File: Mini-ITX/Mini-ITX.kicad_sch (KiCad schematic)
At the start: 8 parts

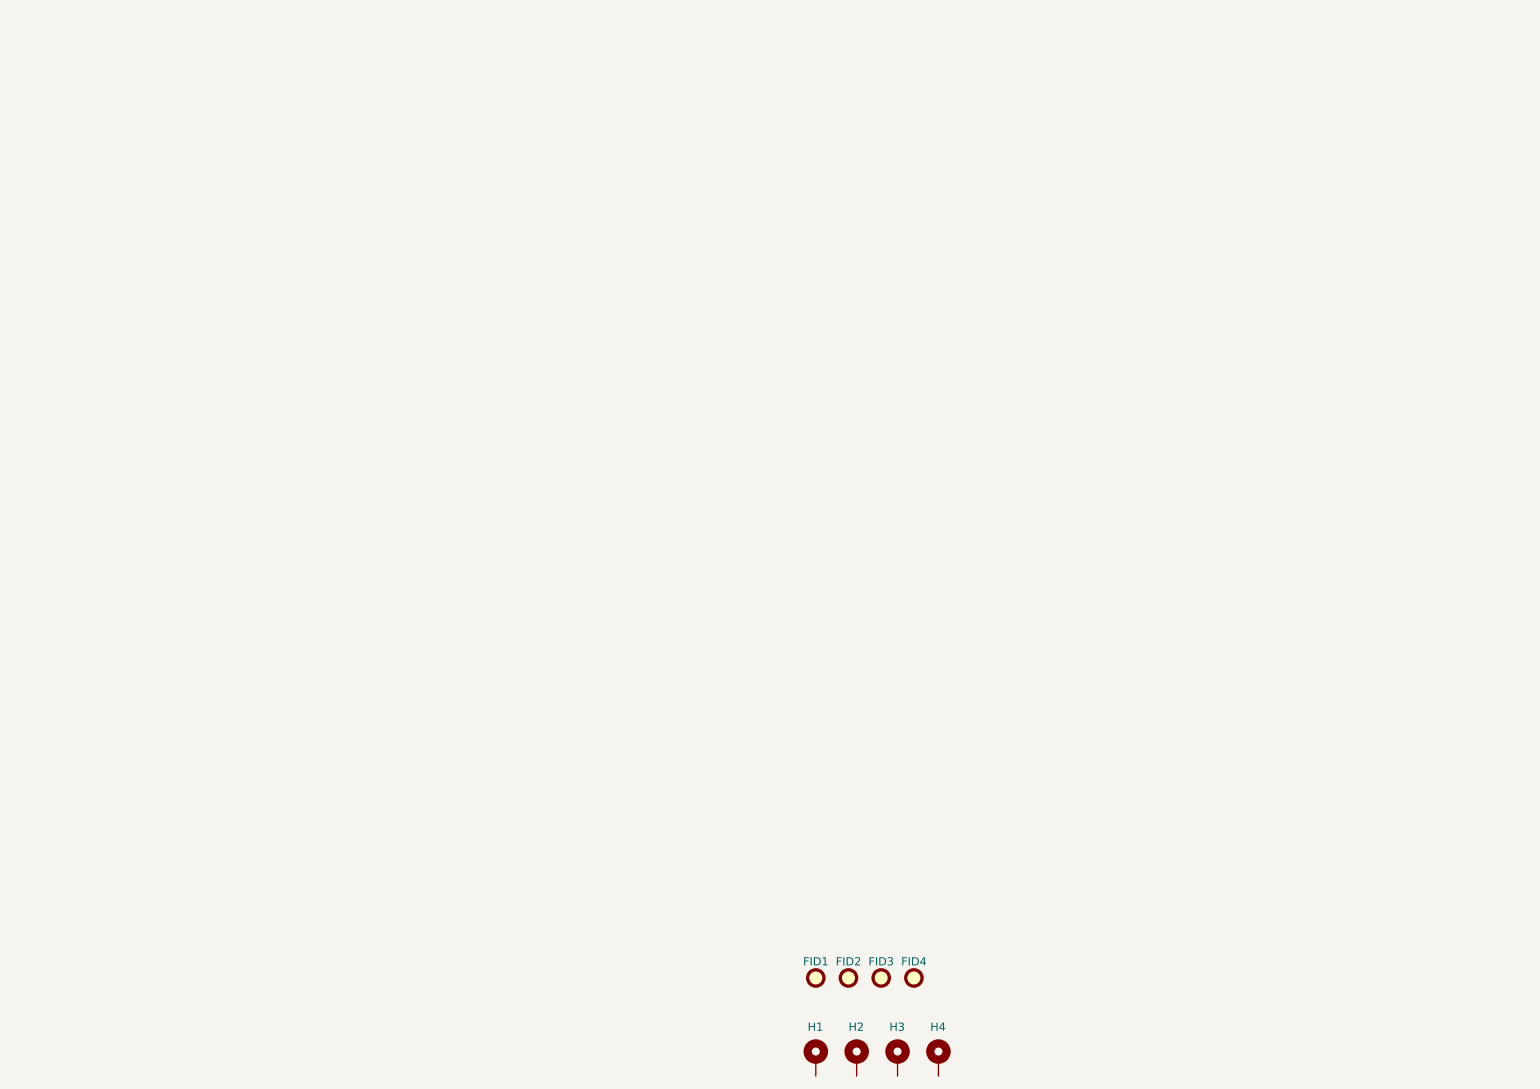
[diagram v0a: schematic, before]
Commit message: add common motherboard connectors
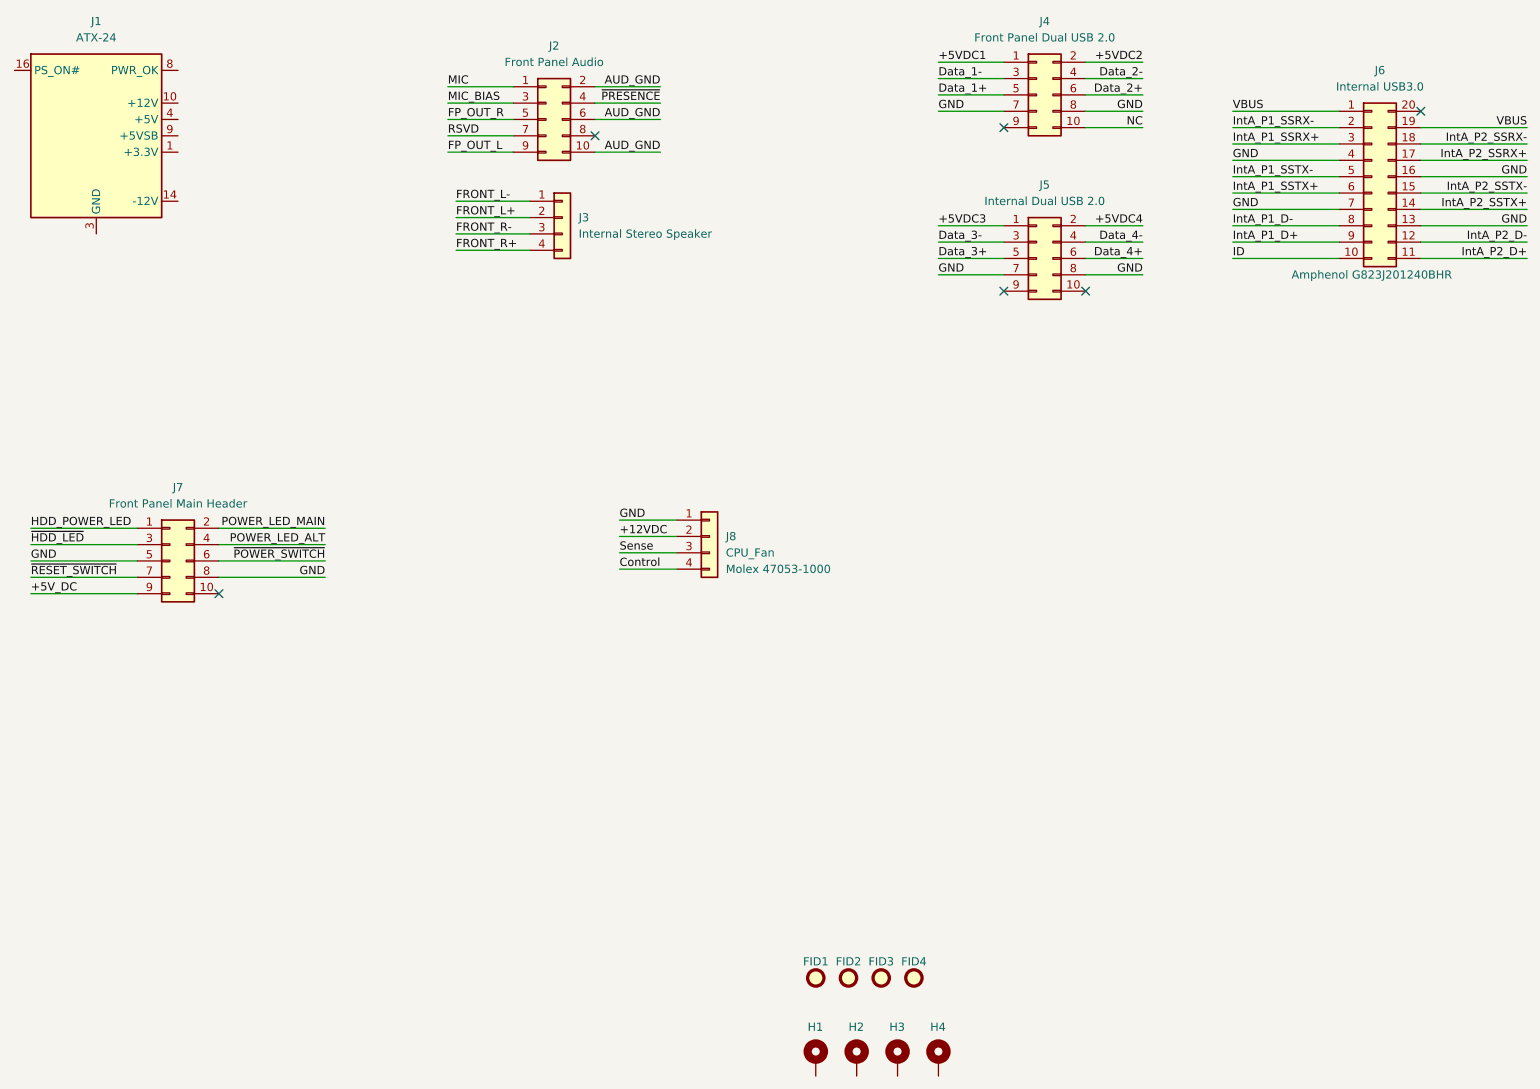
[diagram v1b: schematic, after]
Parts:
- added J1: ATX-24, Connector_Molex:Molex_Mini-Fit_Jr_5566-24A_2x12_P4.20mm_Vertical, symbol Connector:ATX-24
- added J2: Front Panel Audio, Connector_PinHeader_2.54mm:PinHeader_2x05_P2.54mm_Vertical, symbol Connector_Generic:Conn_02x05_Odd_Even
- added J3: Internal Stereo Speaker, Connector_Computer:CS_JS-1125-04_1x04_P2.00mm_Vertical, symbol Connector_Generic:Conn_01x04
- added J4: Front Panel Dual USB 2.0, Connector_PinHeader_2.54mm:PinHeader_2x05_P2.54mm_Vertical, symbol Connector_Generic:Conn_02x05_Odd_Even
- added J5: Internal Dual USB 2.0, Connector_PinHeader_2.54mm:PinHeader_2x05_P2.54mm_Vertical, symbol Connector_Generic:Conn_02x05_Odd_Even
- added J6: Internal USB3.0, Connector_Computer:Amphenol_G823J201xx0xHR_2x10_P2.00mm_Vertical, symbol Connector_Generic:Conn_02x10_Counter_Clockwise
- added J7: Front Panel Main Header, Connector_PinHeader_2.54mm:PinHeader_2x05_P2.54mm_Vertical, symbol Connector_Generic:Conn_02x05_Odd_Even
- added J8: CPU_Fan, Connector:FanPinHeader_1x04_P2.54mm_Vertical, symbol Connector_Generic:Conn_01x04
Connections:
- new net: J1.1 (+3.3V), J1.12 (+3.3V), J1.13 (+3.3V), J1.2 (+3.3V)
- new net: J1.10 (+12V), J1.11 (+12V)
- new net: J1.15 (GND), J1.17 (GND), J1.18 (GND), J1.19 (GND), J1.24 (GND), J1.3 (GND), J1.5 (GND), J1.7 (GND)
- new net: J1.21 (+5V), J1.22 (+5V), J1.23 (+5V), J1.4 (+5V), J1.6 (+5V)
- new net +12VDC: J8.2 (Pin_2)
- new net +5VDC1: J4.1 (Pin_1)
- new net +5VDC2: J4.2 (Pin_2)
- new net +5VDC3: J5.1 (Pin_1)
- new net +5VDC4: J5.2 (Pin_2)
- new net +5V_DC: J7.9 (Pin_9)
- new net AUD_GND: J2.10 (Pin_10), J2.2 (Pin_2), J2.6 (Pin_6)
- new net Control: J8.4 (Pin_4)
- new net Data_1+: J4.5 (Pin_5)
- new net Data_1-: J4.3 (Pin_3)
- new net Data_2+: J4.6 (Pin_6)
- new net Data_2-: J4.4 (Pin_4)
- new net Data_3+: J5.5 (Pin_5)
- new net Data_3-: J5.3 (Pin_3)
- new net Data_4+: J5.6 (Pin_6)
- new net Data_4-: J5.4 (Pin_4)
- new net FP_OUT_L: J2.9 (Pin_9)
- new net FP_OUT_R: J2.5 (Pin_5)
- new net FRONT_L+: J3.2 (Pin_2)
- new net FRONT_L-: J3.1 (Pin_1)
- new net FRONT_R+: J3.4 (Pin_4)
- new net FRONT_R-: J3.3 (Pin_3)
- new net GND: J4.7 (Pin_7), J4.8 (Pin_8), J5.7 (Pin_7), J5.8 (Pin_8), J6.13 (Pin_13), J6.16 (Pin_16), J6.4 (Pin_4), J6.7 (Pin_7), J7.5 (Pin_5), J7.8 (Pin_8), J8.1 (Pin_1)
- new net HDD_POWER_LED: J7.1 (Pin_1)
- new net ID: J6.10 (Pin_10)
- new net IntA_P1_D+: J6.9 (Pin_9)
- new net IntA_P1_D-: J6.8 (Pin_8)
- new net IntA_P1_SSRX+: J6.3 (Pin_3)
- new net IntA_P1_SSRX-: J6.2 (Pin_2)
- new net IntA_P1_SSTX+: J6.6 (Pin_6)
- new net IntA_P1_SSTX-: J6.5 (Pin_5)
- new net IntA_P2_D+: J6.11 (Pin_11)
- new net IntA_P2_D-: J6.12 (Pin_12)
- new net IntA_P2_SSRX+: J6.17 (Pin_17)
- new net IntA_P2_SSRX-: J6.18 (Pin_18)
- new net IntA_P2_SSTX+: J6.14 (Pin_14)
- new net IntA_P2_SSTX-: J6.15 (Pin_15)
- new net MIC: J2.1 (Pin_1)
- new net MIC_BIAS: J2.3 (Pin_3)
- new net NC: J4.10 (Pin_10)
- new net POWER_LED_ALT: J7.4 (Pin_4)
- new net POWER_LED_MAIN: J7.2 (Pin_2)
- new net RSVD: J2.7 (Pin_7)
- new net Sense: J8.3 (Pin_3)
- new net VBUS: J6.1 (Pin_1), J6.19 (Pin_19)
- new net ~{HDD_LED}: J7.3 (Pin_3)
- new net ~{POWER_SWITCH}: J7.6 (Pin_6)
- new net ~{PRESENCE}: J2.4 (Pin_4)
- new net ~{RESET_SWITCH}: J7.7 (Pin_7)
- no-connect marks 0 -> 6
